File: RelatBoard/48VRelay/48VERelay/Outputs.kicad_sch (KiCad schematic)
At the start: 31 parts, among them J10 Screw_Terminal_01x03, J11 Screw_Terminal_01x03, J12 Screw_Terminal_01x03, J13 Screw_Terminal_01x03, J14 Screw_Terminal_01x03, K10 G2RL-1-E, K11 G2RL-1-E, K12 G2RL-1-E, K13 G2RL-1-E, K14 G2RL-1-E, U2 ULN2803A

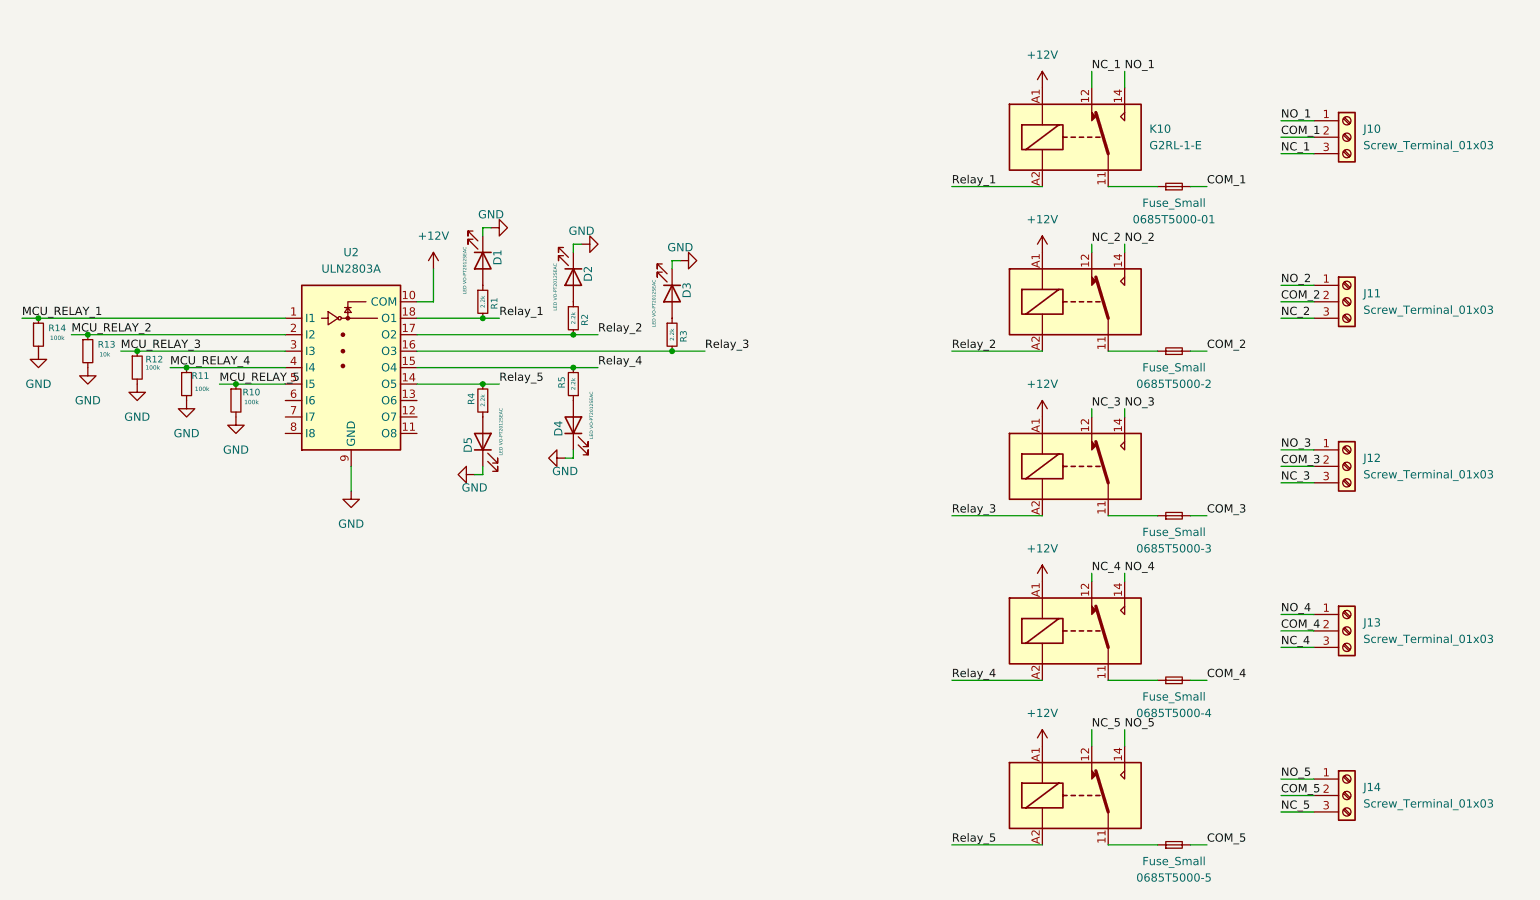
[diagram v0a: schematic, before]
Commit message: JTAG left
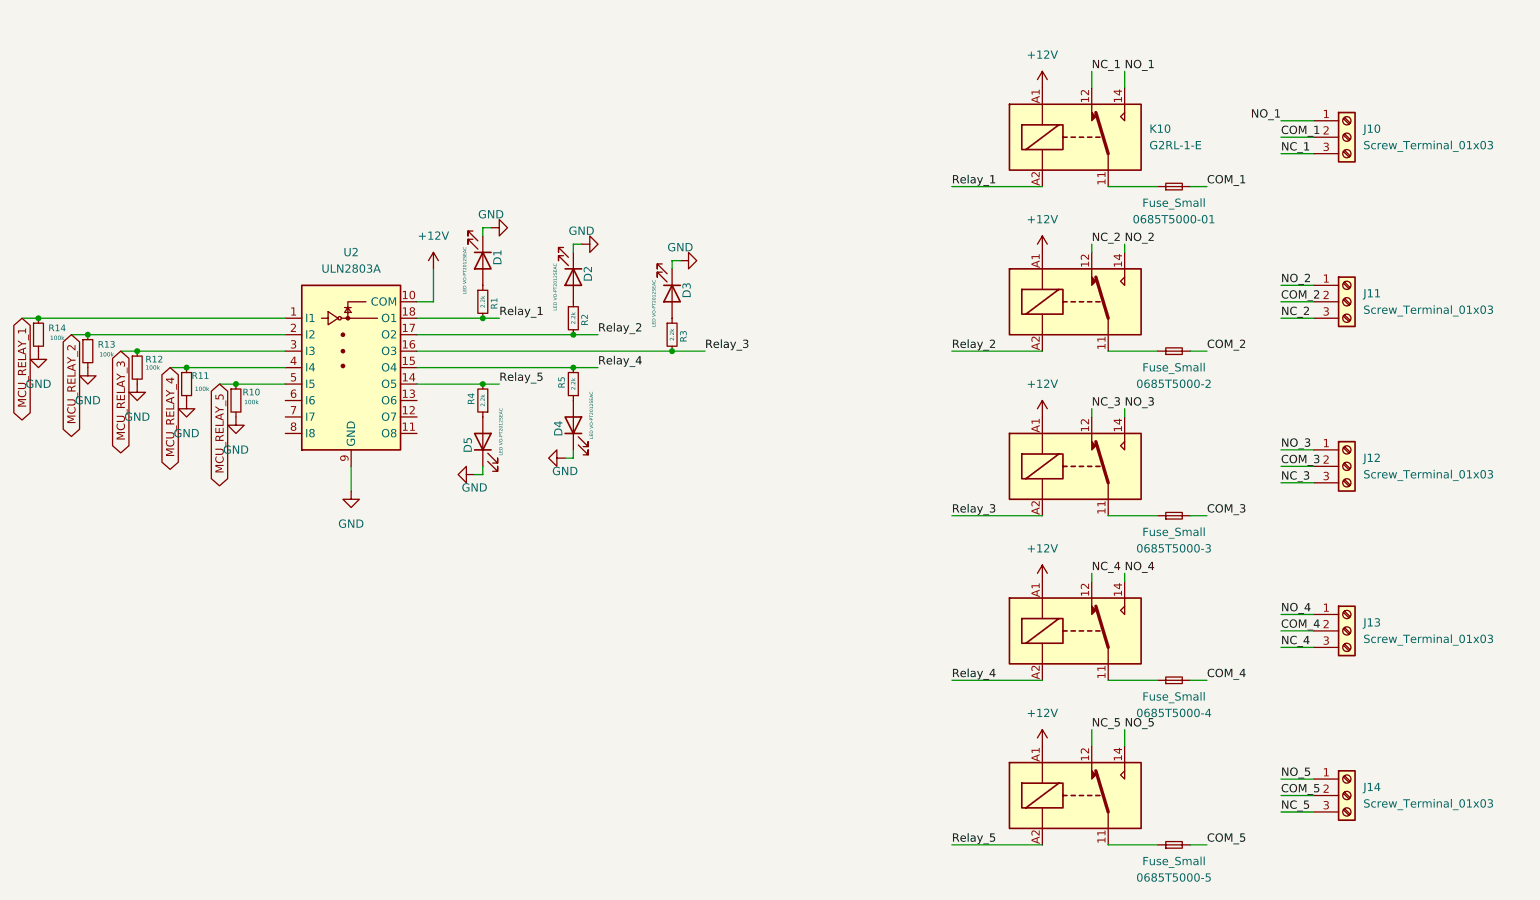
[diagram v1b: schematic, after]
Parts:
- 0685T5000-01, 0685T5000-2, 0685T5000-3, 0685T5000-4, 0685T5000-5: footprint Fuse:Fuse_0603_1608Metric -> Fuse:Fuse_0805_2012Metric
- J10, J11, J12, J13, J14: footprint TerminalBlock:TerminalBlock_Xinya_XY308-2.54-3P_1x03_P2.54mm_Horizontal -> TerminalBlock:TerminalBlock_MaiXu_MX126-5.0-03P_1x03_P5.00mm
- R13: value 10k -> 100k
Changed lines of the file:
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@@
 		)
 	)
-	(label "MCU_RELAY_5"
-		(at 74.93 76.2 0)
-		(effects
-			(font
-				(size 1.27 1.27)
-			)
-			(justify left bottom)
-		)
-	)
 	(label "NO_3"
 		(at 214.63 80.01 0)
@@
 		)
 	)
-	(label "MCU_RELAY_4"
-		(at 67.31 73.66 0)
-		(effects
-			(font
-				(size 1.27 1.27)
-			)
-			(justify left bottom)
-		)
-	)
 	(label "NC_3"
 		(at 209.55 80.01 0)
@@
 		)
 	)
-	(label "NO_1"
-		(at 238.76 35.56 0)
-		(effects
-			(font
-				(size 1.27 1.27)
-			)
-			(justify left bottom)
-		)
-	)
 	(label "COM_5"
 		(at 238.76 139.7 0)
@@
 		)
 	)
-	(label "MCU_RELAY_3"
-		(at 59.69 71.12 0)
-		(effects
-			(font
-				(size 1.27 1.27)
-			)
-			(justify left bottom)
-		)
-	)
 	(label "NO_4"
 		(at 238.76 111.76 0)
@@
 		)
 	)
-	(label "MCU_RELAY_1"
-		(at 44.45 66.04 0)
+	(label "NO_1"
+		(at 214.63 27.94 0)
 		(effects
 			(font
@@
 		)
 	)
-	(label "MCU_RELAY_2"
-		(at 52.07 68.58 0)
-		(effects
-			(font
-				(size 1.27 1.27)
-			)
-			(justify left bottom)
-		)
-	)
 	(label "NC_5"
 		(at 209.55 129.54 0)
@@
 		)
 	)
+	(label "NO_1"
+		(at 238.76 35.56 180)
+		(effects
+			(font
+				(size 1.27 1.27)
+			)
+			(justify right bottom)
+		)
+	)
 	(label "NC_4"
 		(at 238.76 116.84 0)
@@
 		)
 	)
-	(label "NO_1"
-		(at 214.63 27.94 0)
-		(effects
-			(font
-				(size 1.27 1.27)
-			)
-			(justify left bottom)
-		)
-	)
 	(label "NC_3"
 		(at 238.76 91.44 0)
@@
 		)
 	)
+	(global_label "MCU_RELAY_4"
+		(shape bidirectional)
+		(at 67.31 73.66 270)
+		(fields_autoplaced yes)
+		(effects
+			(font
+				(size 1.27 1.27)
+			)
+			(justify right)
+		)
+		(property "Intersheetrefs" "${INTERSHEET_REFS}"
+			(at 67.31 90.5774 90)
+			(hide yes)
+			(show_name no)
+			(do_not_autoplace no)
+			(effects
+				(font
+					(size 1.27 1.27)
+				)
+				(justify right)
+			)
+		)
+	)
+	(global_label "MCU_RELAY_3"
+		(shape bidirectional)
+		(at 59.69 71.12 270)
+		(fields_autoplaced yes)
+		(effects
+			(font
+				(size 1.27 1.27)
+			)
+			(justify right)
+		)
+		(property "Intersheetrefs" "${INTERSHEET_REFS}"
+			(at 59.69 88.0374 90)
+			(hide yes)
+			(show_name no)
+			(do_not_autoplace no)
+			(effects
+				(font
+					(size 1.27 1.27)
+				)
+				(justify right)
+			)
+		)
+	)
+	(global_label "MCU_RELAY_2"
+		(shape bidirectional)
+		(at 52.07 68.58 270)
+		(fields_autoplaced yes)
+		(effects
+			(font
+				(size 1.27 1.27)
+			)
+			(justify right)
+		)
+		(property "Intersheetrefs" "${INTERSHEET_REFS}"
+			(at 52.07 85.4974 90)
+			(hide yes)
+			(show_name no)
+			(do_not_autoplace no)
+			(effects
+				(font
+					(size 1.27 1.27)
+				)
+				(justify right)
+			)
+		)
+	)
+	(global_label "MCU_RELAY_1"
+		(shape bidirectional)
+		(at 44.45 66.04 270)
+		(fields_autoplaced yes)
+		(effects
+			(font
+				(size 1.27 1.27)
+			)
+			(justify right)
+		)
+		(property "Intersheetrefs" "${INTERSHEET_REFS}"
+			(at 44.45 82.9574 90)
+			(hide yes)
+			(show_name no)
+			(do_not_autoplace no)
+			(effects
+				(font
+					(size 1.27 1.27)
+				)
+				(justify right)
+			)
+		)
+	)
+	(global_label "MCU_RELAY_5"
+		(shape bidirectional)
+		(at 74.93 76.2 270)
+		(fields_autoplaced yes)
+		(effects
+			(font
+				(size 1.27 1.27)
+			)
+			(justify right)
+		)
+		(property "Intersheetrefs" "${INTERSHEET_REFS}"
+			(at 74.93 93.1174 90)
+			(hide yes)
+			(show_name no)
+			(do_not_autoplace no)
+			(effects
+				(font
+					(size 1.27 1.27)
+				)
+				(justify right)
+			)
+		)
+	)
 	(symbol
 		(lib_id "Connector:Screw_Terminal_01x03")
@@
 			)
 		)
-		(property "Footprint" "TerminalBlock:TerminalBlock_Xinya_XY308-2.54-3P_1x03_P2.54mm_Horizontal"
+		(property "Footprint" "TerminalBlock:TerminalBlock_MaiXu_MX126-5.0-03P_1x03_P5.00mm"
 			(at 248.92 114.3 0)
 			(hide yes)
@@
 			)
 		)
-		(property "Footprint" "Fuse:Fuse_0603_1608Metric"
+		(property "Footprint" "Fuse:Fuse_0805_2012Metric"
 			(at 222.25 121.92 0)
 			(hide yes)
@@
 			)
 		)
-		(property "Footprint" "Fuse:Fuse_0603_1608Metric"
+		(property "Footprint" "Fuse:Fuse_0805_2012Metric"
 			(at 222.25 96.52 0)
 			(hide yes)
@@
 			)
 		)
-		(property "Footprint" "Fuse:Fuse_0603_1608Metric"
+		(property "Footprint" "Fuse:Fuse_0805_2012Metric"
 			(at 222.25 71.12 0)
 			(hide yes)
@@
 			)
 		)
-		(property "Footprint" "Fuse:Fuse_0603_1608Metric"
+		(property "Footprint" "Fuse:Fuse_0805_2012Metric"
 			(at 222.25 147.32 0)
 			(hide yes)
@@
 			)
 		)
-		(property "Value" "10k"
+		(property "Value" "100k"
 			(at 56.388 71.628 0)
 			(show_name no)
@@
 			)
 		)
-		(property "Footprint" "TerminalBlock:TerminalBlock_Xinya_XY308-2.54-3P_1x03_P2.54mm_Horizontal"
+		(property "Footprint" "TerminalBlock:TerminalBlock_MaiXu_MX126-5.0-03P_1x03_P5.00mm"
 			(at 248.92 88.9 0)
 			(hide yes)
@@
 			)
 		)
-		(property "Footprint" "Fuse:Fuse_0603_1608Metric"
+		(property "Footprint" "Fuse:Fuse_0805_2012Metric"
 			(at 222.25 45.72 0)
 			(hide yes)
@@
 			)
 		)
-		(property "Footprint" "TerminalBlock:TerminalBlock_Xinya_XY308-2.54-3P_1x03_P2.54mm_Horizontal"
+		(property "Footprint" "TerminalBlock:TerminalBlock_MaiXu_MX126-5.0-03P_1x03_P5.00mm"
 			(at 248.92 139.7 0)
 			(hide yes)
@@
 			)
 		)
-		(property "Footprint" "TerminalBlock:TerminalBlock_Xinya_XY308-2.54-3P_1x03_P2.54mm_Horizontal"
+		(property "Footprint" "TerminalBlock:TerminalBlock_MaiXu_MX126-5.0-03P_1x03_P5.00mm"
 			(at 248.92 38.1 0)
 			(hide yes)
@@
 			)
 		)
-		(property "Footprint" "TerminalBlock:TerminalBlock_Xinya_XY308-2.54-3P_1x03_P2.54mm_Horizontal"
+		(property "Footprint" "TerminalBlock:TerminalBlock_MaiXu_MX126-5.0-03P_1x03_P5.00mm"
 			(at 248.92 63.5 0)
 			(hide yes)

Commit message: wired uart and jtag
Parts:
- F1: renamed from 0685T5000-01; value Fuse_Small -> 0685T5000
- F2: renamed from 0685T5000-2; value Fuse_Small -> 0685T5000
- F3: renamed from 0685T5000-3; value Fuse_Small -> 0685T5000-01
- F4: renamed from 0685T5000-4; value Fuse_Small -> 0685T5000-01
- F5: renamed from 0685T5000-5; value Fuse_Small -> 0685T5000
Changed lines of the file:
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@@
 		(in_pos_files yes)
 		(dnp no)
-		(property "Reference" "0685T5000-4"
+		(property "Reference" "F4"
 			(at 222.25 127 0)
 			(show_name no)
@@
 			)
 		)
-		(property "Value" "Fuse_Small"
+		(property "Value" "0685T5000-01"
 			(at 222.25 124.46 0)
 			(show_name no)
@@
 			(project "48VERelay"
 				(path "/2d740e7a-a48e-41b8-b74e-ca0ab277f7d9/9acca724-bbf8-479c-b765-a30537109626"
-					(reference "0685T5000-4")
+					(reference "F4")
 					(unit 1)
 				)
@@
 		(in_pos_files yes)
 		(dnp no)
-		(property "Reference" "0685T5000-3"
+		(property "Reference" "F3"
 			(at 222.25 101.6 0)
 			(show_name no)
@@
 			)
 		)
-		(property "Value" "Fuse_Small"
+		(property "Value" "0685T5000-01"
 			(at 222.25 99.06 0)
 			(show_name no)
@@
 			(project "48VERelay"
 				(path "/2d740e7a-a48e-41b8-b74e-ca0ab277f7d9/9acca724-bbf8-479c-b765-a30537109626"
-					(reference "0685T5000-3")
+					(reference "F3")
 					(unit 1)
 				)
@@
 		(in_pos_files yes)
 		(dnp no)
-		(property "Reference" "0685T5000-2"
+		(property "Reference" "F2"
 			(at 222.25 76.2 0)
 			(show_name no)
@@
 			)
 		)
-		(property "Value" "Fuse_Small"
+		(property "Value" "0685T5000"
 			(at 222.25 73.66 0)
 			(show_name no)
@@
 			(project "48VERelay"
 				(path "/2d740e7a-a48e-41b8-b74e-ca0ab277f7d9/9acca724-bbf8-479c-b765-a30537109626"
-					(reference "0685T5000-2")
+					(reference "F2")
 					(unit 1)
 				)
@@
 		(in_pos_files yes)
 		(dnp no)
-		(property "Reference" "0685T5000-5"
+		(property "Reference" "F5"
 			(at 222.25 152.4 0)
 			(show_name no)
@@
 			)
 		)
-		(property "Value" "Fuse_Small"
+		(property "Value" "0685T5000"
 			(at 222.25 149.86 0)
 			(show_name no)
@@
 			(project "48VERelay"
 				(path "/2d740e7a-a48e-41b8-b74e-ca0ab277f7d9/9acca724-bbf8-479c-b765-a30537109626"
-					(reference "0685T5000-5")
+					(reference "F5")
 					(unit 1)
 				)
@@
 		(in_pos_files yes)
 		(dnp no)
-		(property "Reference" "0685T5000-01"
+		(property "Reference" "F1"
 			(at 222.25 50.8 0)
 			(show_name no)
@@
 			)
 		)
-		(property "Value" "Fuse_Small"
+		(property "Value" "0685T5000"
 			(at 222.25 48.26 0)
 			(show_name no)
@@
 			(project "48VERelay"
 				(path "/2d740e7a-a48e-41b8-b74e-ca0ab277f7d9/9acca724-bbf8-479c-b765-a30537109626"
-					(reference "0685T5000-01")
-					(unit 1)
-				)
+					(reference "F1")
+					(unit 1)
+				)

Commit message: Order1
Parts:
- D1, D2, D3, D4, D5: footprint LED_SMD:LED_0201_0603Metric -> LED_SMD:LED_0805_2012Metric
- F1, F2, F3, F4, F5: footprint Fuse:Fuse_0805_2012Metric -> Fuse:Fuse_1206_3216Metric
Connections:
- net +12V: now also D1.2 (A), D2.2 (A), D3.2 (A), D4.2 (A), D5.2 (A)
- net GND: no longer D1.1 (K), D2.1 (K), D3.1 (K), D4.1 (K), D5.1 (K)
- net at R2.1: now also D2.1 (K); no longer D2.2 (A)
- net at R5.1: now also D4.1 (K); no longer D4.2 (A)
- net at R4.1: now also D5.1 (K); no longer D5.2 (A)
- net at R3.1: now also D3.1 (K); no longer D3.2 (A)
- net at R1.1: now also D1.1 (K); no longer D1.2 (A)
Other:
- moved on the sheet: D1, D2, D3, D4, D5

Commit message: Final design
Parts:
- removed F1, F2, F5: 0685T5000, Fuse:Fuse_1206_3216Metric, symbol Device:Fuse_Small
- removed F3, F4: 0685T5000-01, Fuse:Fuse_1206_3216Metric, symbol Device:Fuse_Small
- removed K10, K11, K12, K13, K14: G2RL-1-E, Relay_THT:Relay_SPDT_Omron_G2RL-1-E, symbol Relay:G2RL-1-E
- added K1, K2, K3, K4, K5: G2R-1-E DC12, RELAY_G2R-1-E AC12_OMR, symbol g2r-1-e:G2R-1-E_DC12
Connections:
- net +12V: now also K1.1, K2.1, K3.1, K4.1, K5.1
- net COM_1: now also K1.3, K1.6
- net COM_2: now also K2.3, K2.6
- net COM_3: now also K3.3, K3.6
- net COM_4: now also K4.3, K4.6
- net COM_5: now also K5.3, K5.6
- net NC_1: now also K1.2, K1.7
- net NC_2: now also K2.2, K2.7
- net NC_3: now also K3.2, K3.7
- net NC_4: now also K4.2, K4.7
- net NC_5: now also K5.2, K5.7
- net NO_1: now also K1.4, K1.5
- net NO_2: now also K2.4, K2.5
- net NO_3: now also K3.4, K3.5
- net NO_4: now also K4.4, K4.5
- net NO_5: now also K5.4, K5.5
- net Relay_1: now also K1.8
- net Relay_2: now also K2.8
- net Relay_3: now also K3.8
- net Relay_4: now also K4.8
- net Relay_5: now also K5.8
